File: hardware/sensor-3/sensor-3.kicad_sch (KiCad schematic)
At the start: 12 parts, among them J101 2x05_Horizontal, U101 A31010SEHALT-10

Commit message: Update sensors
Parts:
- C101: footprint Capacitor_SMD:C_0603_1608Metric -> V2_Capacitor_SMD:C_0603; symbol Device:C_Small -> V2_Device:C_0603_0u1; Manufacturer (none) -> TDK; Mouser (none) -> 810-CGA3E2X7R1H104MA; Product (none) -> CGA3E2X7R1H104M080AA; Rating (none) -> 50V
- FID101, FID102: value Fiducial -> Fiducial_Paste
- INFO101: value ORDER-NUMBER -> Order_Number
- J101: Manufacturer (none) -> Amphenol FCI; Mouser (none) -> 649-200211120001T4LF; Product (none) -> 20021112-00010T4LF
- U101: Manufacturer (none) -> Allegro MicroSystems; Mouser (none) -> 250-A31010SEHALT-10; Product (none) -> A31010SEHALT-10
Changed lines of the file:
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@@
 	)
 	(symbol
-		(lib_id "power:+3V3")
+		(lib_id "V2_power:+3V3")
 		(at 194.31 81.28 270)
 		(unit 1)
@@
 			)
 		)
-		(property "Description" "Power symbol creates a global label with name \"+3V3\""
+		(property "Description" ""
 			(at 194.31 81.28 0)
 			(effects
@@
 	)
 	(symbol
-		(lib_id "power:+3V3")
+		(lib_id "V2_power:+3V3")
 		(at 200.66 107.95 270)
 		(unit 1)
@@
 			)
 		)
-		(property "Description" "Power symbol creates a global label with name \"+3V3\""
+		(property "Description" ""
 			(at 200.66 107.95 0)
 			(effects
@@
 	)
 	(symbol
-		(lib_id "power:+3V3")
+		(lib_id "V2_power:+3V3")
 		(at 85.09 64.77 0)
 		(unit 1)
@@
 			)
 		)
-		(property "Description" "Power symbol creates a global label with name \"+3V3\""
+		(property "Description" ""
 			(at 85.09 64.77 0)
 			(effects
@@
 	)
 	(symbol
-		(lib_id "power:GND")
+		(lib_id "V2_power:GND")
 		(at 194.31 77.47 90)
 		(unit 1)
@@
 			)
 		)
-		(property "Description" "Power symbol creates a global label with name \"GND\" , ground"
+		(property "Description" ""
 			(at 194.31 77.47 0)
 			(effects
@@
 	)
 	(symbol
-		(lib_id "power:+3V3")
+		(lib_id "V2_power:+3V3")
 		(at 116.84 72.39 270)
 		(mirror x)
@@
 			)
 		)
-		(property "Description" "Power symbol creates a global label with name \"+3V3\""
+		(property "Description" ""
 			(at 116.84 72.39 0)
 			(effects
@@
 			)
 		)
-		(property "Datasheet" "~"
+		(property "Datasheet" ""
 			(at 193.04 102.87 0)
 			(effects
@@
 			)
 		)
-		(property "Description" ""
+		(property "Description" "Amphenol – Minitek127"
 			(at 194.31 102.87 0)
 			(effects
@@
 			)
 		)
-		(property "Sim.Enable" "0"
-			(at 194.31 102.87 0)
+		(property "Mouser" "649-200211120001T4LF"
+			(at 194.31 125.73 0)
+			(effects
+				(font
+					(size 1.27 1.27)
+				)
+				(hide yes)
+			)
+		)
+		(property "Manufacturer" "Amphenol FCI"
+			(at 194.31 120.65 0)
+			(effects
+				(font
+					(size 1.27 1.27)
+				)
+				(hide yes)
+			)
+		)
+		(property "Product" "20021112-00010T4LF"
+			(at 194.31 123.19 0)
 			(effects
 				(font
@@
 	)
 	(symbol
-		(lib_id "Device:C_Small")
+		(lib_id "V2_Device:C_0603_0u1")
 		(at 85.09 67.31 0)
 		(unit 1)
@@
 			)
 		)
-		(property "Footprint" "Capacitor_SMD:C_0603_1608Metric"
+		(property "Footprint" "V2_Capacitor_SMD:C_0603"
 			(at 85.09 67.31 0)
 			(effects
@@
 			)
 		)
-		(property "Datasheet" "~"
+		(property "Datasheet" ""
 			(at 85.09 67.31 0)
 			(effects
@@
 			)
 		)
+		(property "Mouser" "810-CGA3E2X7R1H104MA"
+			(at 85.09 87.63 0)
+			(effects
+				(font
+					(size 1.27 1.27)
+				)
+				(hide yes)
+			)
+		)
+		(property "Manufacturer" "TDK"
+			(at 85.09 82.55 0)
+			(effects
+				(font
+					(size 1.27 1.27)
+				)
+				(hide yes)
+			)
+		)
+		(property "Product" "CGA3E2X7R1H104M080AA"
+			(at 85.09 85.09 0)
+			(effects
+				(font
+					(size 1.27 1.27)
+				)
+				(hide yes)
+			)
+		)
+		(property "Rating" "50V"
+			(at 85.09 90.17 0)
+			(effects
+				(font
+					(size 1.27 1.27)
+				)
+				(hide yes)
+			)
+		)
 		(pin "1"
 		)
@@
 	)
 	(symbol
-		(lib_id "power:GND")
+		(lib_id "V2_power:GND")
 		(at 187.96 107.95 270)
 		(unit 1)
@@
 			)
 		)
-		(property "Description" "Power symbol creates a global label with name \"GND\" , ground"
+		(property "Description" ""
 			(at 187.96 107.95 0)
 			(effects
@@
 			)
 		)
-		(property "Value" "ORDER-NUMBER"
+		(property "Value" "Order_Number"
 			(at 240.03 177.8 0)
 			(effects
@@
 			)
 		)
-		(property "Sim.Enable" "0"
-			(at 240.03 175.26 0)
-			(effects
-				(font
-					(size 1.27 1.27)
-				)
-				(hide yes)
-			)
-		)
 		(instances
 			(project "cube-cover"
@@
 			)
 		)
-		(property "Value" "Fiducial"
+		(property "Value" "Fiducial_Paste"
 			(at 265.43 171.45 0)
 			(effects
@@
 					(size 1.27 1.27)
 				)
+				(hide yes)
 			)
 		)
@@
 			)
 		)
-		(property "Sim.Enable" "0"
-			(at 265.43 175.26 0)
-			(effects
-				(font
-					(size 1.27 1.27)
-				)
-				(hide yes)
-			)
-		)
 		(instances
 			(project "ring"
@@
 	)
 	(symbol
-		(lib_id "power:GND")
+		(lib_id "V2_power:GND")
 		(at 85.09 69.85 0)
 		(unit 1)
@@
 			)
 		)
-		(property "Description" "Power symbol creates a global label with name \"GND\" , ground"
+		(property "Description" ""
 			(at 85.09 69.85 0)
 			(effects
@@
 			)
 		)
+		(property "Manufacturer" "Allegro MicroSystems"
+			(at 111.76 88.9 0)
+			(effects
+				(font
+					(size 1.27 1.27)
+				)
+				(hide yes)
+			)
+		)
+		(property "Product" "A31010SEHALT-10"
+			(at 111.76 91.44 0)
+			(effects
+				(font
+					(size 1.27 1.27)
+				)
+				(hide yes)
+			)
+		)
+		(property "Mouser" "250-A31010SEHALT-10"
+			(at 111.76 93.98 0)
+			(effects
+				(font
+					(size 1.27 1.27)
+				)
+				(hide yes)
+			)
+		)
 		(pin "6"
 		)
@@
 	)
 	(symbol
-		(lib_id "power:PWR_FLAG")
+		(lib_id "V2_power:PWR_FLAG")
 		(at 194.31 81.28 90)
 		(unit 1)
@@
 			)
 		)
-		(property "Datasheet" "~"
+		(property "Datasheet" ""
 			(at 194.31 81.28 0)
 			(effects
@@
 	)
 	(symbol
-		(lib_id "power:GND")
+		(lib_id "V2_power:GND")
 		(at 116.84 74.93 90)
 		(mirror x)
@@
 				)
 				(justify left)
+				(hide yes)
 			)
 		)
@@
 			)
 		)
-		(property "Description" "Power symbol creates a global label with name \"GND\" , ground"
+		(property "Description" ""
 			(at 116.84 74.93 0)
 			(effects
@@
 			)
 		)
-		(property "Value" "Fiducial"
+		(property "Value" "Fiducial_Paste"
 			(at 274.32 171.45 0)
 			(effects
@@
 					(size 1.27 1.27)
 				)
+				(hide yes)
 			)
 		)
@@
 		)
 		(property "Description" "Fiducial Marker"
-			(at 274.32 175.26 0)
-			(effects
-				(font
-					(size 1.27 1.27)
-				)
-				(hide yes)
-			)
-		)
-		(property "Sim.Enable" "0"
 			(at 274.32 175.26 0)
 			(effects
@@
 	)
 	(symbol
-		(lib_id "power:+3V3")
+		(lib_id "V2_power:+3V3")
 		(at 116.84 59.69 270)
 		(mirror x)
@@
 			)
 		)
-		(property "Description" "Power symbol creates a global label with name \"+3V3\""
+		(property "Description" ""
 			(at 116.84 59.69 0)
 			(effects
@@
 	)
 	(symbol
-		(lib_id "power:PWR_FLAG")
+		(lib_id "V2_power:PWR_FLAG")
 		(at 194.31 77.47 90)
 		(unit 1)
@@
 			)
 		)
-		(property "Datasheet" "~"
+		(property "Datasheet" ""
 			(at 194.31 77.47 0)
 			(effects

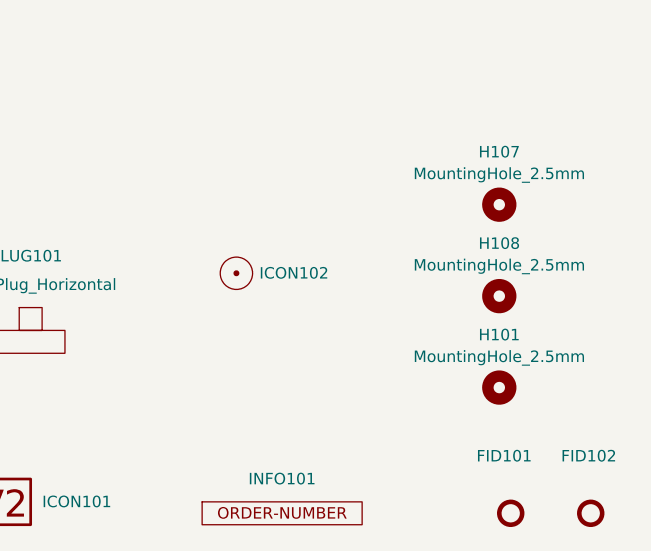
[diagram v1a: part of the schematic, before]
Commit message: Replace Order_Number
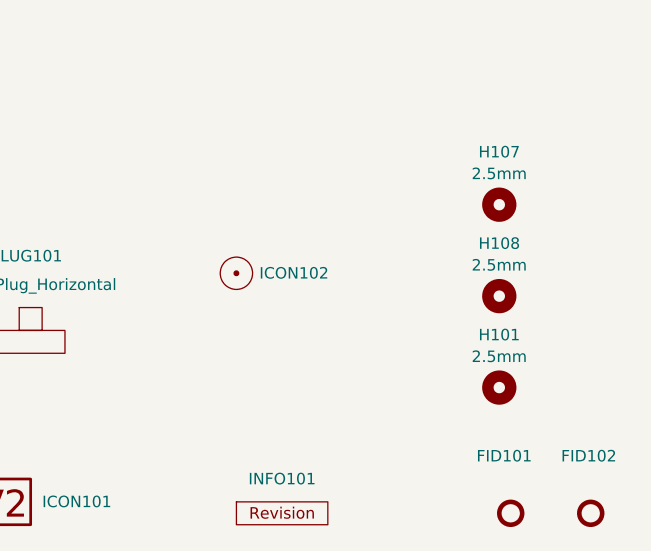
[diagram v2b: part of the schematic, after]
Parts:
- H101, H107, H108: value MountingHole_2.5mm -> 2.5mm
- INFO101: value Order_Number -> ~; footprint V2_Production:Order_Number -> V2_Production:Revision; symbol V2_Production:Order_Number -> V2_Production:Revision
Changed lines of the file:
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@@
 	(title_block
 		(title "V2 sax")
-		(date "2025-12-05")
-		(rev "1")
+		(date "2026-02-13")
+		(rev "2026-02-13")
 		(company "Versio Duo")
 		(comment 1 "Sensor 1")
@@
 			)
 		)
-		(property "Value" "MountingHole_2.5mm"
+		(property "Value" "2.5mm"
 			(at 264.16 147.701 0)
 			(effects
@@
 		)
 		(property "Description" "Mounting Hole without connection"
-			(at 264.16 151.13 0)
-			(effects
-				(font
-					(size 1.27 1.27)
-				)
-				(hide yes)
-			)
-		)
-		(property "Sim.Enable" "0"
 			(at 264.16 151.13 0)
 			(effects
@@
 			)
 		)
-		(property "Value" "MountingHole_2.5mm"
+		(property "Value" "2.5mm"
 			(at 264.16 157.861 0)
 			(effects
@@
 		)
 		(property "Description" "Mounting Hole without connection"
-			(at 264.16 161.29 0)
-			(effects
-				(font
-					(size 1.27 1.27)
-				)
-				(hide yes)
-			)
-		)
-		(property "Sim.Enable" "0"
 			(at 264.16 161.29 0)
 			(effects
@@
 	)
 	(symbol
-		(lib_id "V2_Production:Order_Number")
+		(lib_id "V2_Production:Revision")
 		(at 240.03 175.26 0)
 		(unit 1)
@@
 			)
 		)
-		(property "Value" "Order_Number"
+		(property "Value" "~"
 			(at 240.03 177.8 0)
 			(effects
@@
 			)
 		)
-		(property "Footprint" "V2_Production:Order_Number"
+		(property "Footprint" "V2_Production:Revision"
 			(at 240.03 180.34 0)
 			(effects
@@
 			)
 		)
-		(property "Value" "MountingHole_2.5mm"
+		(property "Value" "2.5mm"
 			(at 264.16 137.541 0)
 			(effects
@@
 		)
 		(property "Description" "Mounting Hole without connection"
-			(at 264.16 140.97 0)
-			(effects
-				(font
-					(size 1.27 1.27)
-				)
-				(hide yes)
-			)
-		)
-		(property "Sim.Enable" "0"
 			(at 264.16 140.97 0)
 			(effects
@@
 			(at 209.55 173.99 0)
 			(effects
-				(font
-					(size 1.27 1.27)
-				)
-				(hide yes)
-			)
-		)
-		(property "Sim.Enable" "0"
-			(at 209.55 173.99 0)
-			(effects

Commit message: Update Library
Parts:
- C101: symbol V2_Device:C_0603_0u1 -> V2_Capacitor:0603_0u1
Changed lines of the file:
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@@
 		(dnp no)
 		(fields_autoplaced yes)
-		(property "Reference" "#PWR0108"
+		(property "Reference" "#PWR108"
 			(at 190.5 81.28 0)
 			(effects
@@
 			(project ""
 				(path "/6c8448b4-b04d-47e1-934e-e40cbe27a7be"
-					(reference "#PWR0108")
+					(reference "#PWR108")
 					(unit 1)
 				)
@@
 		(dnp no)
 		(fields_autoplaced yes)
-		(property "Reference" "#PWR0116"
+		(property "Reference" "#PWR116"
 			(at 196.85 107.95 0)
 			(effects
@@
 			(project "sensor-1"
 				(path "/6c8448b4-b04d-47e1-934e-e40cbe27a7be"
-					(reference "#PWR0116")
+					(reference "#PWR116")
 					(unit 1)
 				)
@@
 		(dnp no)
 		(fields_autoplaced yes)
-		(property "Reference" "#PWR0102"
+		(property "Reference" "#PWR102"
 			(at 85.09 68.58 0)
 			(effects
@@
 			(project "sensor-1"
 				(path "/6c8448b4-b04d-47e1-934e-e40cbe27a7be"
-					(reference "#PWR0102")
+					(reference "#PWR102")
 					(unit 1)
 				)
@@
 		(on_board yes)
 		(dnp no)
-		(property "Reference" "#PWR0107"
+		(property "Reference" "#PWR107"
 			(at 200.66 77.47 0)
 			(effects
@@
 			(project "ring"
 				(path "/6c8448b4-b04d-47e1-934e-e40cbe27a7be"
-					(reference "#PWR0107")
+					(reference "#PWR107")
 					(unit 1)
 				)
@@
 		(dnp no)
 		(fields_autoplaced yes)
-		(property "Reference" "#PWR0104"
+		(property "Reference" "#PWR104"
 			(at 113.03 72.39 0)
 			(effects
@@
 			(project "sensor-1"
 				(path "/6c8448b4-b04d-47e1-934e-e40cbe27a7be"
-					(reference "#PWR0104")
+					(reference "#PWR104")
 					(unit 1)
 				)
@@
 	)
 	(symbol
-		(lib_id "V2_Device:C_0603_0u1")
+		(lib_id "V2_Capacitor:0603_0u1")
 		(at 85.09 67.31 0)
 		(unit 1)
@@
 		(on_board yes)
 		(dnp no)
-		(property "Reference" "#PWR0115"
+		(property "Reference" "#PWR115"
 			(at 181.61 107.95 0)
 			(effects
@@
 			(project "sensor-1"
 				(path "/6c8448b4-b04d-47e1-934e-e40cbe27a7be"
-					(reference "#PWR0115")
+					(reference "#PWR115")
 					(unit 1)
 				)
@@
 		(on_board yes)
 		(dnp no)
-		(property "Reference" "#PWR0103"
+		(property "Reference" "#PWR103"
 			(at 85.09 76.2 0)
 			(effects
@@
 			(project "sensor-1"
 				(path "/6c8448b4-b04d-47e1-934e-e40cbe27a7be"
-					(reference "#PWR0103")
+					(reference "#PWR103")
 					(unit 1)
 				)
@@
 		(on_board yes)
 		(dnp no)
-		(property "Reference" "#FLG0102"
+		(property "Reference" "#FLG102"
 			(at 192.405 81.28 0)
 			(effects
@@
 			(project "ring"
 				(path "/6c8448b4-b04d-47e1-934e-e40cbe27a7be"
-					(reference "#FLG0102")
+					(reference "#FLG102")
 					(unit 1)
 				)
@@
 		(on_board yes)
 		(dnp no)
-		(property "Reference" "#PWR0105"
+		(property "Reference" "#PWR105"
 			(at 123.19 74.93 0)
 			(effects
@@
 			(project "sensor-1"
 				(path "/6c8448b4-b04d-47e1-934e-e40cbe27a7be"
-					(reference "#PWR0105")
+					(reference "#PWR105")
 					(unit 1)
 				)
@@
 		(dnp no)
 		(fields_autoplaced yes)
-		(property "Reference" "#PWR0101"
+		(property "Reference" "#PWR101"
 			(at 113.03 59.69 0)
 			(effects
@@
 			(project "sensor-1"
 				(path "/6c8448b4-b04d-47e1-934e-e40cbe27a7be"
-					(reference "#PWR0101")
+					(reference "#PWR101")
 					(unit 1)
 				)
@@
 		(on_board yes)
 		(dnp no)
-		(property "Reference" "#FLG0101"
+		(property "Reference" "#FLG101"
 			(at 192.405 77.47 0)
 			(effects
@@
 			(project "ring"
 				(path "/6c8448b4-b04d-47e1-934e-e40cbe27a7be"
-					(reference "#FLG0101")
-					(unit 1)
-				)
+					(reference "#FLG101")
+					(unit 1)
+				)

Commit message: Export stencil
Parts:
- INFO101: value ~ -> (none)
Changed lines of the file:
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@@
 	(title_block
 		(title "V2 sax")
-		(date "2026-02-13")
+		(date "2026-02-25")
 		(rev "2026-02-13")
 		(company "Versio Duo")
@@
 			)
 		)
-		(property "Value" "~"
+		(property "Value" ""
 			(at 240.03 177.8 0)
 			(effects

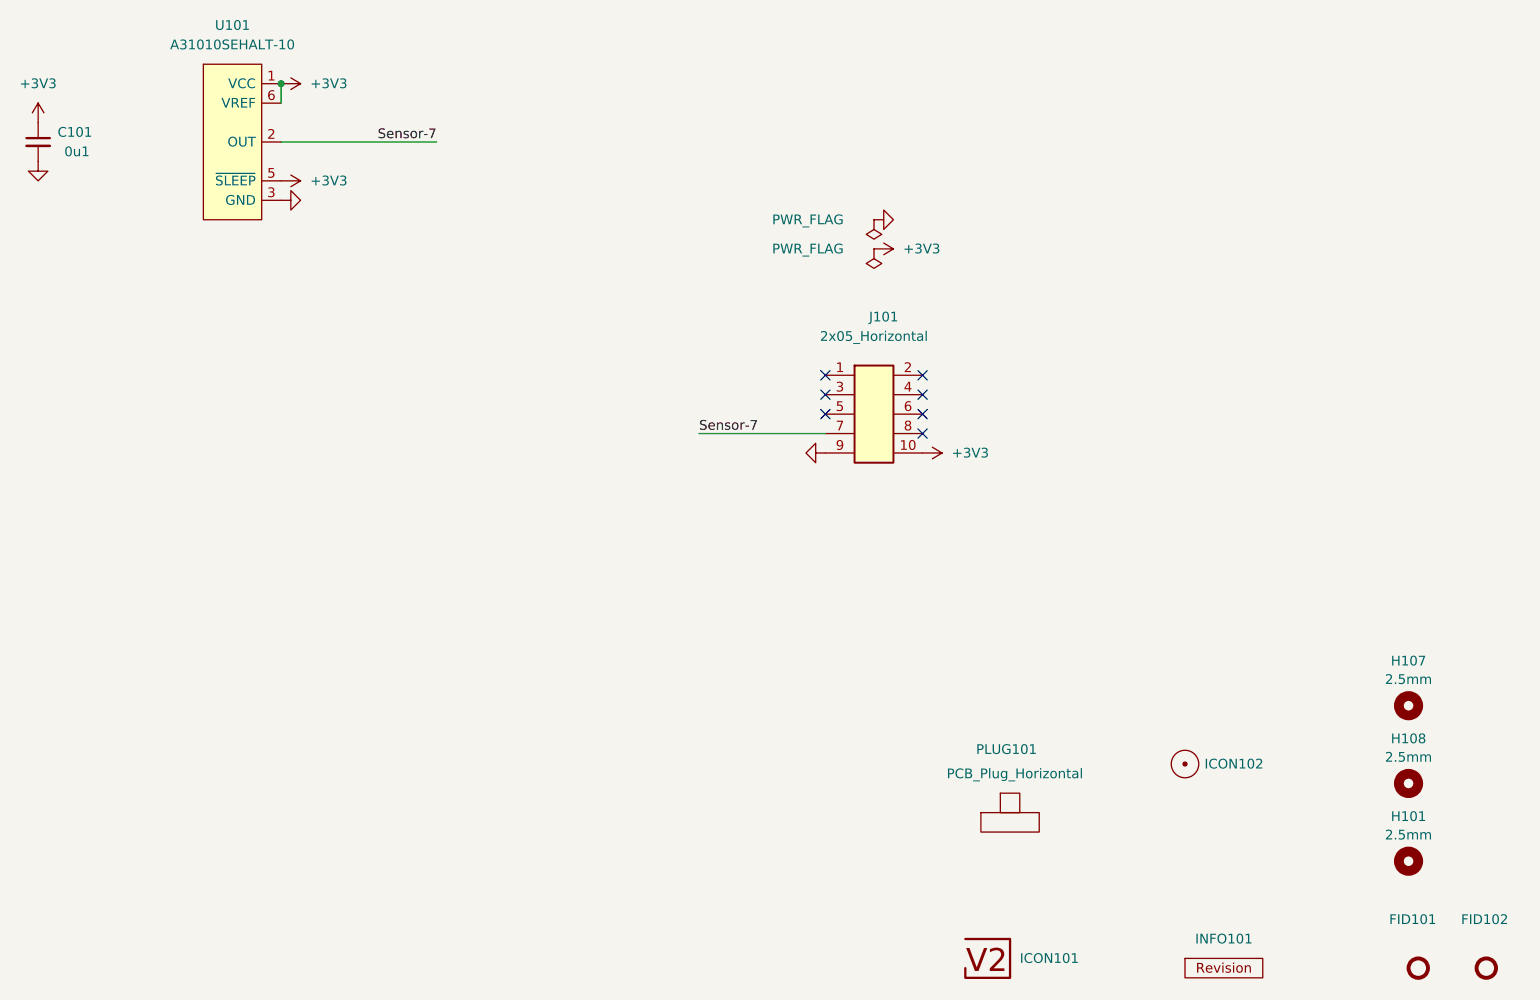
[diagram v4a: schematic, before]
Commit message: KiCad 10
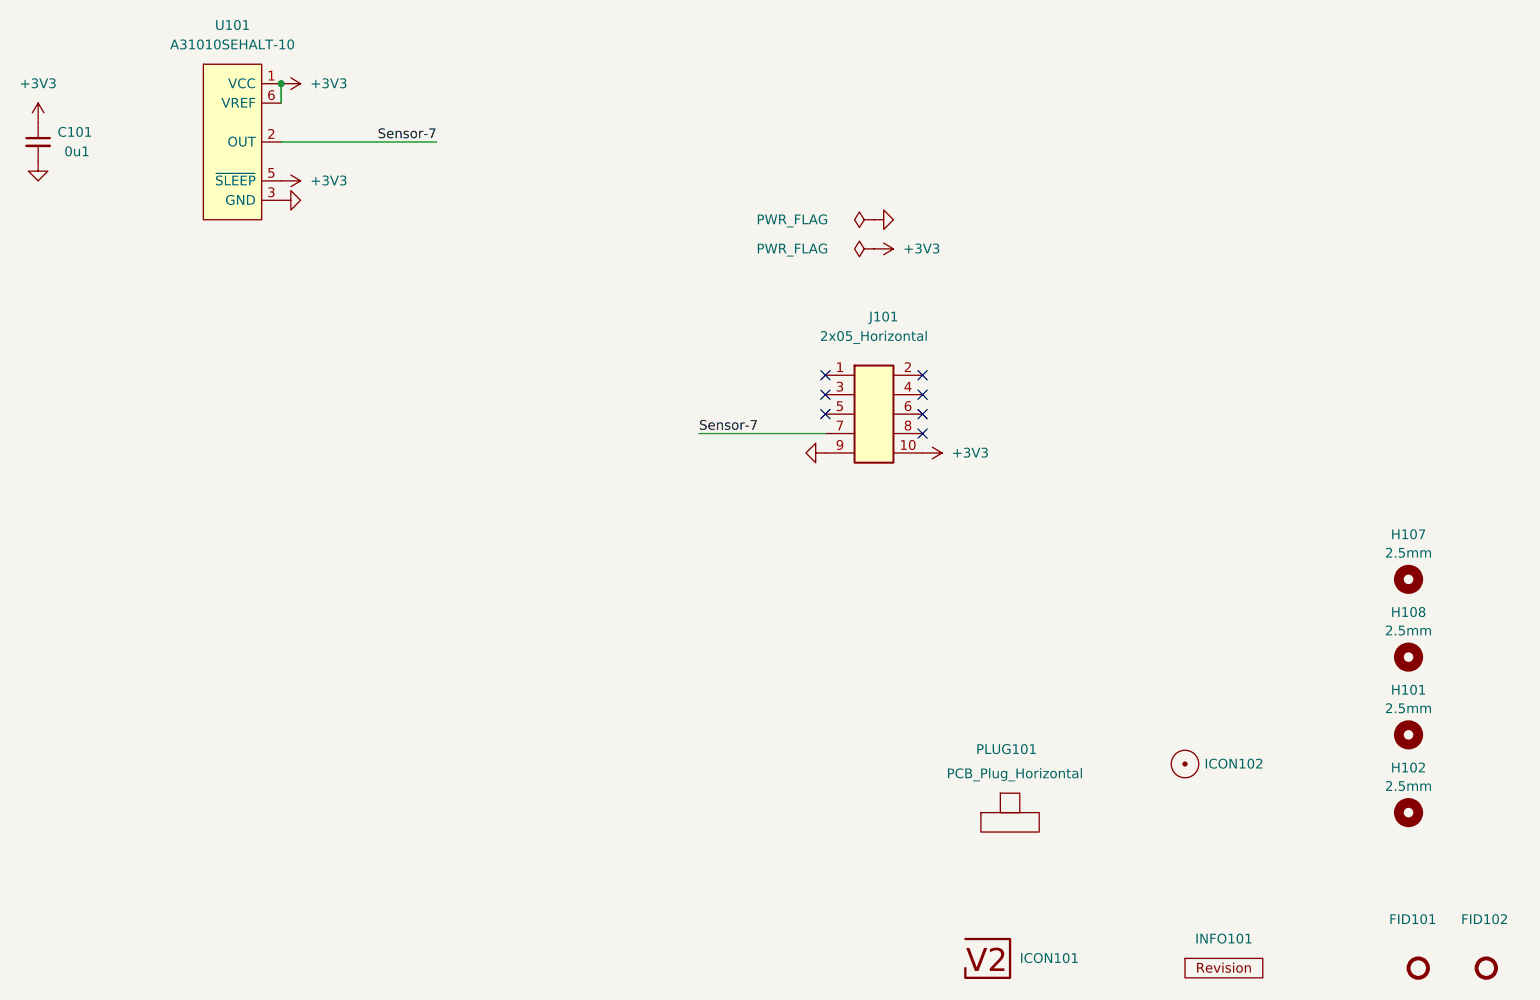
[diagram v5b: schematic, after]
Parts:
- added H102: 2.5mm, V2_Mechanical:MountingHole_2.5mm, symbol V2_Mechanical:MountingHole_2.5mm
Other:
- moved on the sheet: H101, H107, H108

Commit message: Good Bye Imperial
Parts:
- C101: footprint V2_Capacitor_SMD:C_0603 -> V2_Capacitor_SMD:C_1608; symbol V2_Capacitor:0603_0u1 -> V2_Capacitor:1608_0u1
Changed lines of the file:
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@@
 	)
 	(symbol
-		(lib_id "V2_Capacitor:0603_0u1")
+		(lib_id "V2_Capacitor:1608_0u1")
 		(at 85.09 67.31 0)
 		(unit 1)
@@
 			)
 		)
-		(property "Footprint" "V2_Capacitor_SMD:C_0603"
+		(property "Footprint" "V2_Capacitor_SMD:C_1608"
 			(at 85.09 67.31 0)
 			(hide yes)
